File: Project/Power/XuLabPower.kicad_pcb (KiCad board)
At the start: 8 copper layers, 74 x 148 mm, 179 parts, among them J1 Servo, J10 Battery, J11 Battery, J12 Battery, J13 I2C, J14 SWD, J15 SPI1, J16 5V_2A, J17 5V_6A, J2 Servo, J3 Servo, J4 Servo, J5 Servo, J6 Servo, J7 Servo, J8 Servo, J9 Battery, Q1 SQJ138ELP, Q2 SQJ138ELP, Q3 SQJ138ELP, Q4 SQJ138ELP, Q5 SQJ138ELP, Q6 SQJ138ELP, SW1 SW_Push, U1 LM74502, U10 INA199B3DCKR, U11 TL331, U12 INA199B3DCKR, U13 TL331, U14 STM32L422KBTx, U15 TPS560200, U16 MIC5219-3.3YM5, U17 TPS562200, U18 TPS54627, U19 INA226, U2 NCV68061, U20 INA226, U21 INA226, U22 INA226, U23 INA226, U24 INA226, U25 INA226, U26 INA226, U3 NCV68061, U4 INA199B3DCKR, U5 TL331, U6 INA199B3DCKR, U7 TL331, U8 NCV68061, U9 NCV68061

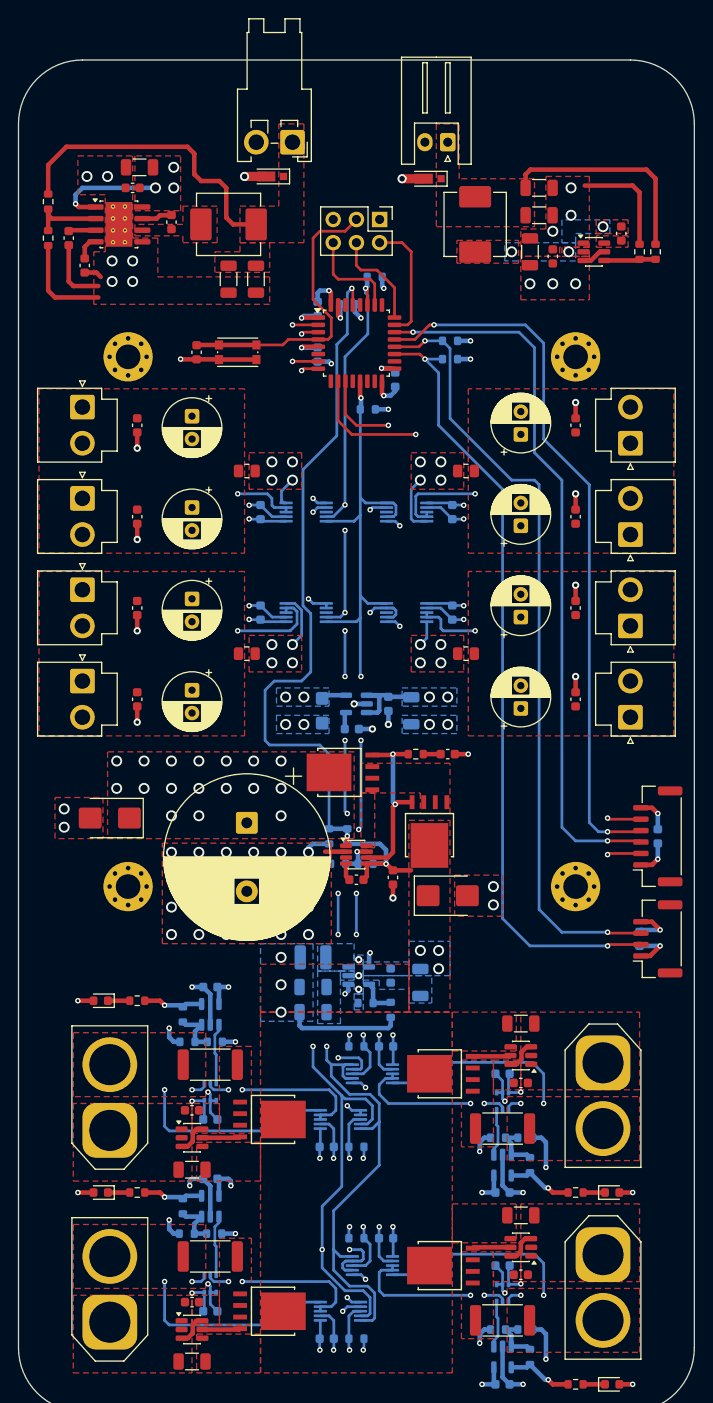
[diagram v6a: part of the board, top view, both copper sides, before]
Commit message: Shorten board length
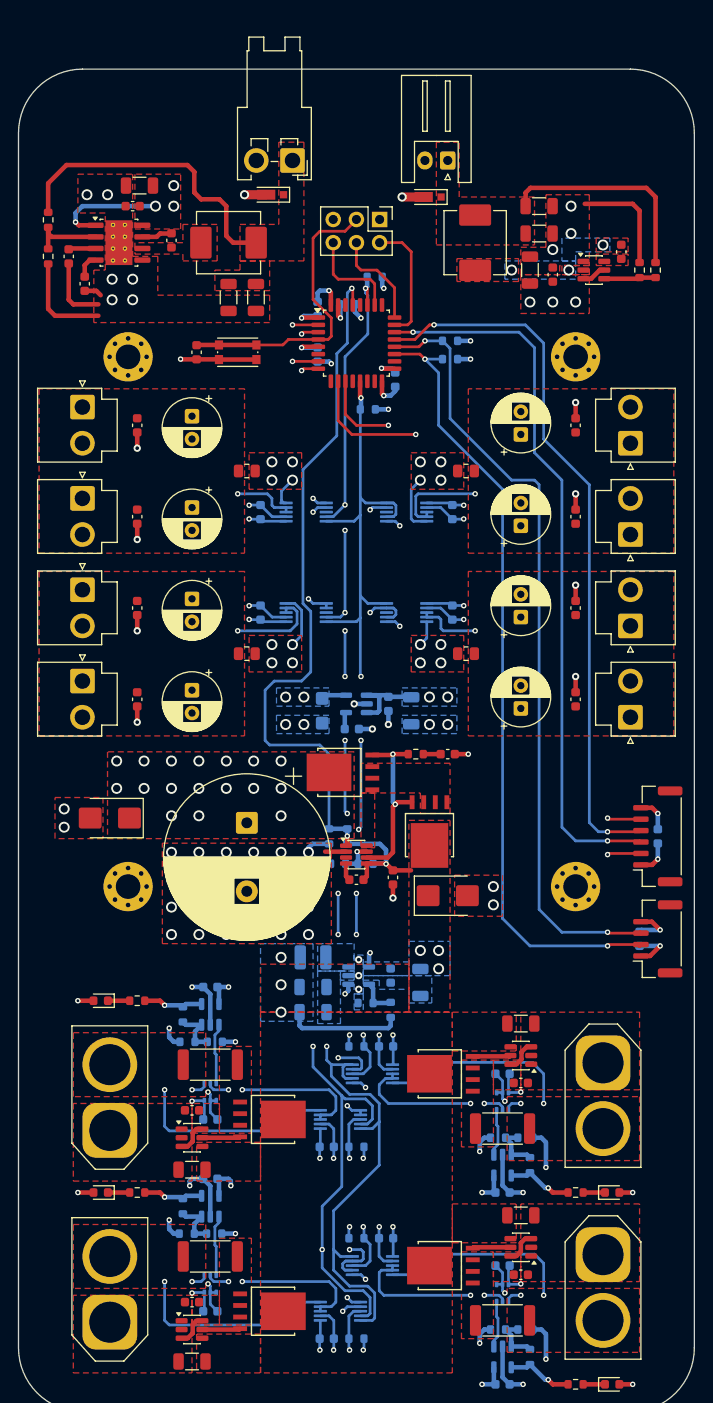
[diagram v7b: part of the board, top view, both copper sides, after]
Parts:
- moved C26 2.00 mm to (167.0, 39.0)
- moved C27 2.00 mm to (169.5, 39.5)
- moved C28 2.00 mm to (177.0, 37.0)
- moved C29 2.00 mm to (168.0, 32.0)
- moved C30 2.00 mm to (168.0, 35.0)
- moved C32 2.00 mm to (124.2, 29.8)
- moved C33 2.00 mm to (123.5, 32.0)
- moved C34 2.00 mm to (116.5, 37.5)
- moved C35 2.00 mm to (118.2, 40.5)
- moved C36 2.00 mm to (127.8, 35.8)
- moved C37 2.00 mm to (134.0, 42.0)
- moved C38 2.00 mm to (137.0, 42.0)
- moved D5 2.00 mm to (156.2, 31.0)
- moved D6 2.00 mm to (139.0, 30.8)
- moved J16 2.00 mm to (158.0, 27.0)
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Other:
- board size 74 x 148 mm -> 74 x 147 mm
